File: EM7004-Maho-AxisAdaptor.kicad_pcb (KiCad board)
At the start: 2 copper layers, 41.6 x 119.2 mm, 6 parts, among them J1 1830498, J2 1830498, J3 D-SUB-DR-15PCM-CB, J4 D-SUB-DR-15PCM-CB, J5 DMR-9S, J6 XY2500R-D-5.08-2P

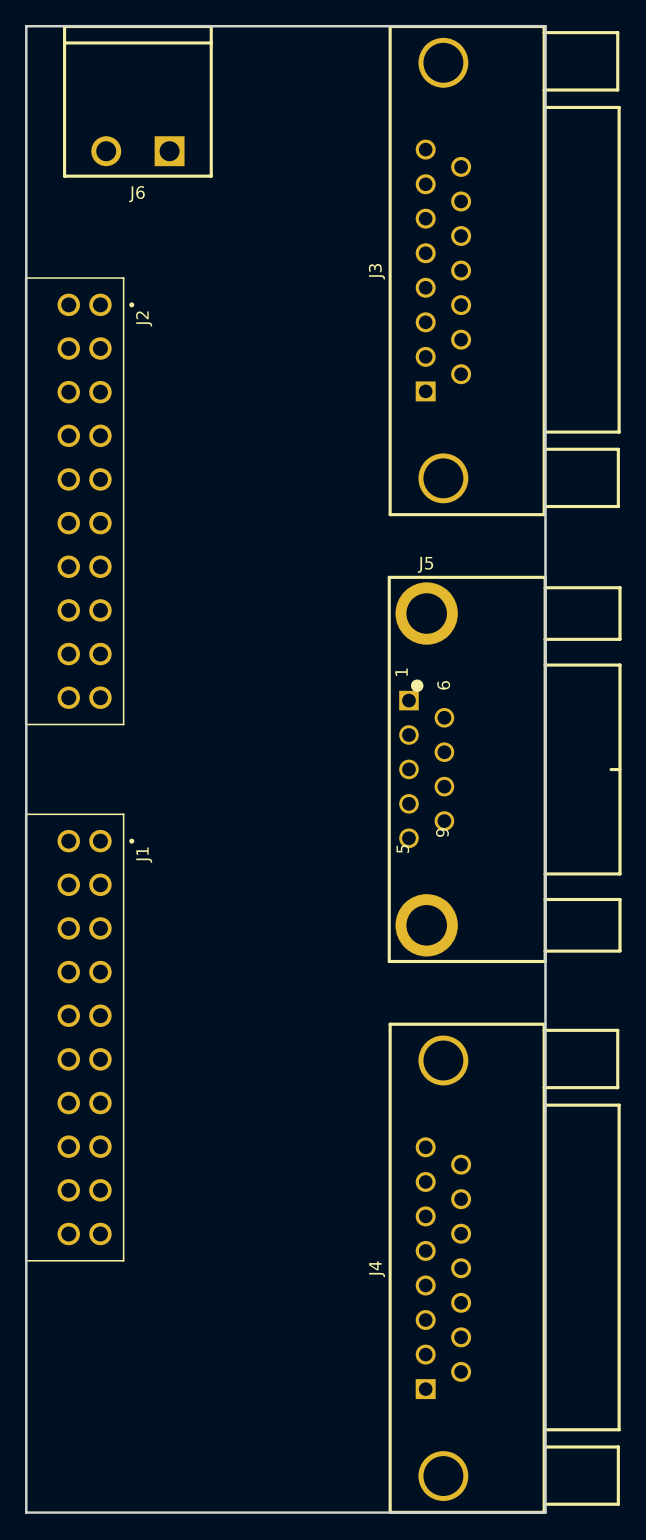
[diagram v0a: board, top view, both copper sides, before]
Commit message: added 5V regulator
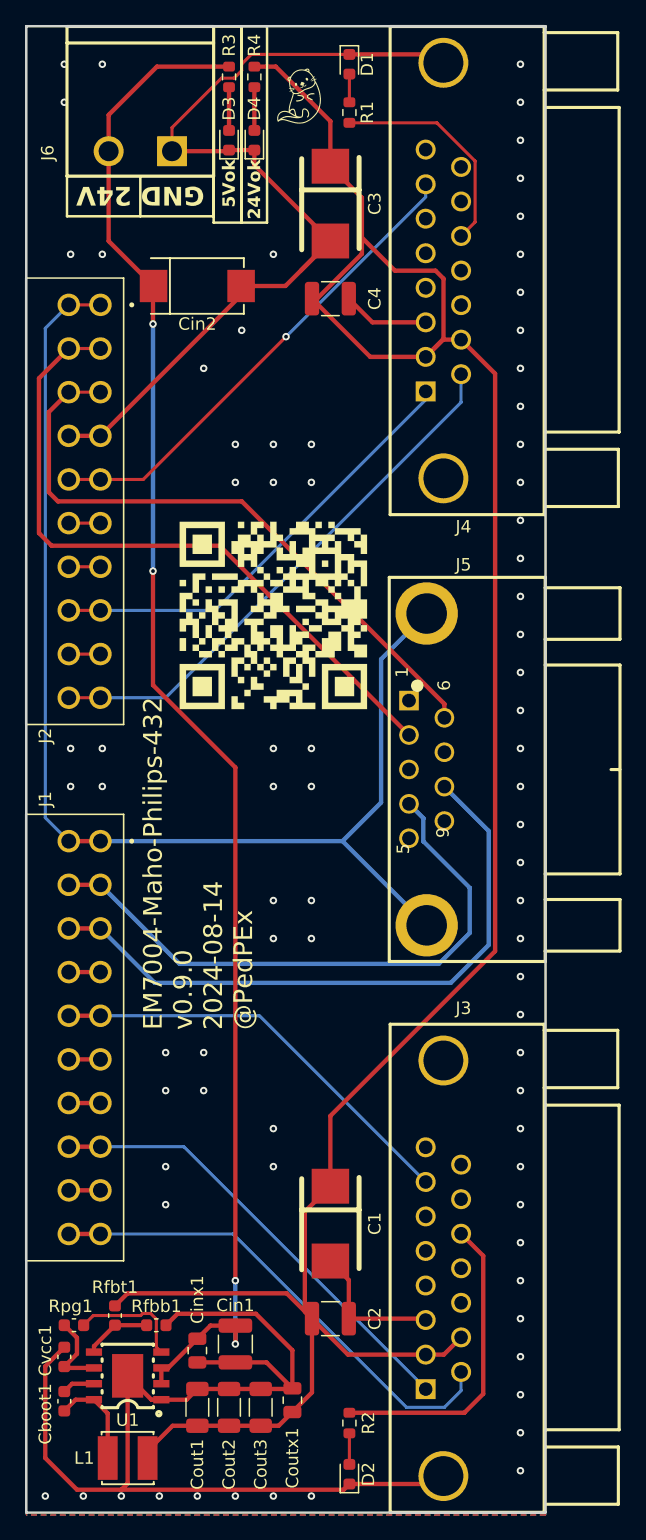
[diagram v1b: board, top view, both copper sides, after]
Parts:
- added C1: 100u, easyeda2kicad:CASE-D_7343, F.Cu at (81.0, 125.8)
- added C2: 10u, Capacitor_SMD:C_1210_3225Metric, F.Cu at (81.0, 133.4)
- added C3: 100u, easyeda2kicad:CASE-D_7343, F.Cu at (81.0, 44.0)
- added C4: 10u, Capacitor_SMD:C_1210_3225Metric, F.Cu at (81.0, 51.7)
- added Cboot1: 100n, Capacitor_SMD:C_0603_1608Metric, F.Cu at (59.7, 140.1)
- added Cin1: 10u, Capacitor_SMD:C_1210_3225Metric, F.Cu at (73.4, 135.5)
- added Cin2: 10u, easyeda2kicad:CAP-SMD_L7.3-W4.3-R-RD, F.Cu at (70.4, 50.6)
- added Cinx1: 220n, Capacitor_SMD:C_0805_2012Metric, F.Cu at (70.4, 136.0)
- added Cout1: 47u, Capacitor_SMD:C_1206_3216Metric, F.Cu at (70.4, 140.6)
- added Cout2: 47u, Capacitor_SMD:C_1206_3216Metric, F.Cu at (72.9, 140.6)
- added Cout3: 47u, Capacitor_SMD:C_1206_3216Metric, F.Cu at (75.4, 140.6)
- added Coutx1: 100n, Capacitor_SMD:C_0805_2012Metric, F.Cu at (78.0, 140.0)
- added Cvcc1: 1u, Capacitor_SMD:C_0603_1608Metric, F.Cu at (59.7, 136.5)
- added D1: LED, LED_SMD:LED_0603_1608Metric, F.Cu at (82.6, 32.9)
- added D2: LED, LED_SMD:LED_0603_1608Metric, F.Cu at (82.6, 145.9)
- added D3: LED, LED_SMD:LED_0603_1608Metric, F.Cu at (72.9, 39.0)
- added D4: LED, LED_SMD:LED_0603_1608Metric, F.Cu at (74.9, 39.0)
- added G***: LOGO, LOGO, F.Cu at (76.5, 77.1)
- added G***: LOGO, LOGO, F.Cu at (78.5, 35.4)
- added L1: APSWPA4018S100MTF, easyeda2kicad:IND-SMD_L4.0-W4.0, F.Cu at (64.8, 144.6)
- added R1: 220, Resistor_SMD:R_0603_1608Metric, F.Cu at (82.6, 36.7)
- added R2: 220, Resistor_SMD:R_0603_1608Metric, F.Cu at (82.6, 141.8)
- added R3: 2k4, Resistor_SMD:R_0603_1608Metric, F.Cu at (72.9, 33.9)
- added R4: 220, Resistor_SMD:R_0603_1608Metric, F.Cu at (74.9, 33.9)
- added Rfbb1: 24k9, Capacitor_SMD:C_0603_1608Metric, F.Cu at (67.1, 134.0)
- added Rfbt1: 100k, Capacitor_SMD:C_0603_1608Metric, F.Cu at (63.8, 133.2)
- added Rpg1: 100k, Capacitor_SMD:C_0603_1608Metric, F.Cu at (60.5, 134.0)
- added U1: LMR33630ADDAR, easyeda2kicad:ESOP-8_L4.9-W3.9-P1.27-LS6.0-TL-EP, F.Cu at (64.8, 138.0)
- moved J6 0.19 mm to (65.8, 39.8)
- renumbered J4 to J3, J3 to J4
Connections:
- J3 pad 1: unconnected-(J4-Pad1) -> 0_EncoderB
- J3 pad 10: unconnected-(J4-Pad10) -> +5V
- J3 pad 13: unconnected-(J4-Pad13) -> Net-(J3-Pad13)
- J3 pad 7: unconnected-(J4-Pad7) -> 0_EncoderLatch
- J3 pad 9: unconnected-(J4-Pad9) -> 0_EncoderA
- J4 pad 1: unconnected-(J3-Pad1) -> 1_EncoderB
- J4 pad 10: unconnected-(J3-Pad10) -> +5V
- J4 pad 13: unconnected-(J3-Pad13) -> Net-(J4-Pad13)
- J4 pad 7: unconnected-(J3-Pad7) -> 1_EncoderLatch
- J4 pad 9: unconnected-(J3-Pad9) -> 1_EncoderA
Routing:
- net +5V: track 0.00 -> 193.0 mm
- net GND: track 0.00 -> 185.2 mm, vias 0 -> 80
- net +24V: track 0.00 -> 124.1 mm, vias 0 -> 4
- net 0_Shield: track 0.00 -> 99.6 mm
- net 1_Analog-: track 0.00 -> 54.7 mm
- net 1_Analog+: track 0.00 -> 51.1 mm
- net 0_Analog+: track 0.00 -> 50.9 mm
- net 0_Analog-: track 0.00 -> 48.2 mm
- net 1_EncoderA: track 0.00 -> 43.5 mm
- net 0_EncoderA: track 0.00 -> 39.3 mm
- net 1_EncoderLatch: track 0.00 -> 39.0 mm, vias 0 -> 1
- net 0_EncoderB: track 0.00 -> 36.7 mm
- net 1_EncoderB: track 0.00 -> 36.3 mm
- net 0_EncoderLatch: track 0.00 -> 34.1 mm
- net Net-(J3-Pad13): track 0.00 -> 24.9 mm
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- added copper zone on B.Cu, net GND
- added copper zone on F.Cu, net GND
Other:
- board text added: "${TITLE} ${REVISION} ${ISSUE_DATE} @PedPEx"
- board text added: "24Vok"
- board text added: "5Vok"
- board text added: "GND 24V"
